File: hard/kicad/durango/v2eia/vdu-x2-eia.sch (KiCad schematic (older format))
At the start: 42 parts, among them Q4 BC548, Q5 BC548, U124 74HC574, U125 74HC157, U126 74HC86, U127 74HC245, U15 74HC4040, U16 74HC02, U17 74HC21, U18 74HC85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

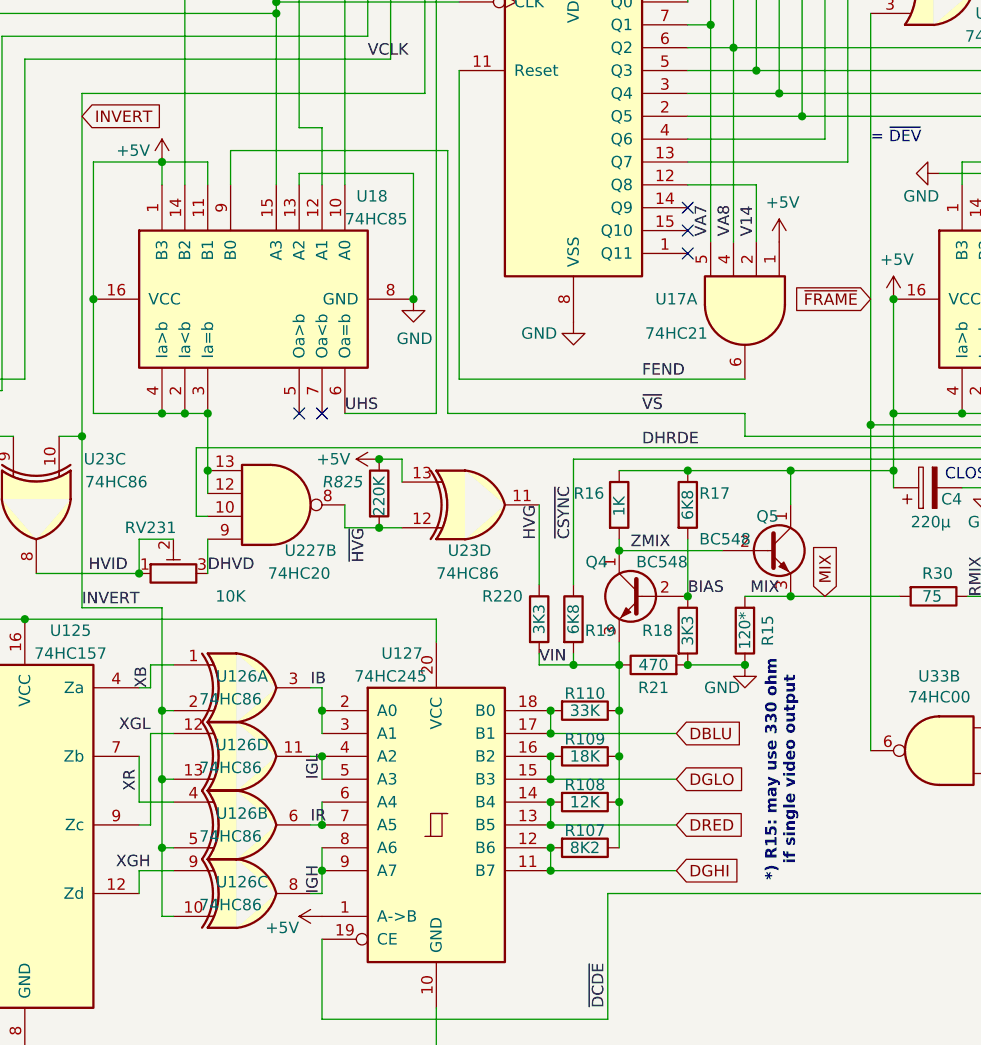
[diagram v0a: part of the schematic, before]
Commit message: fix EIA v2.2
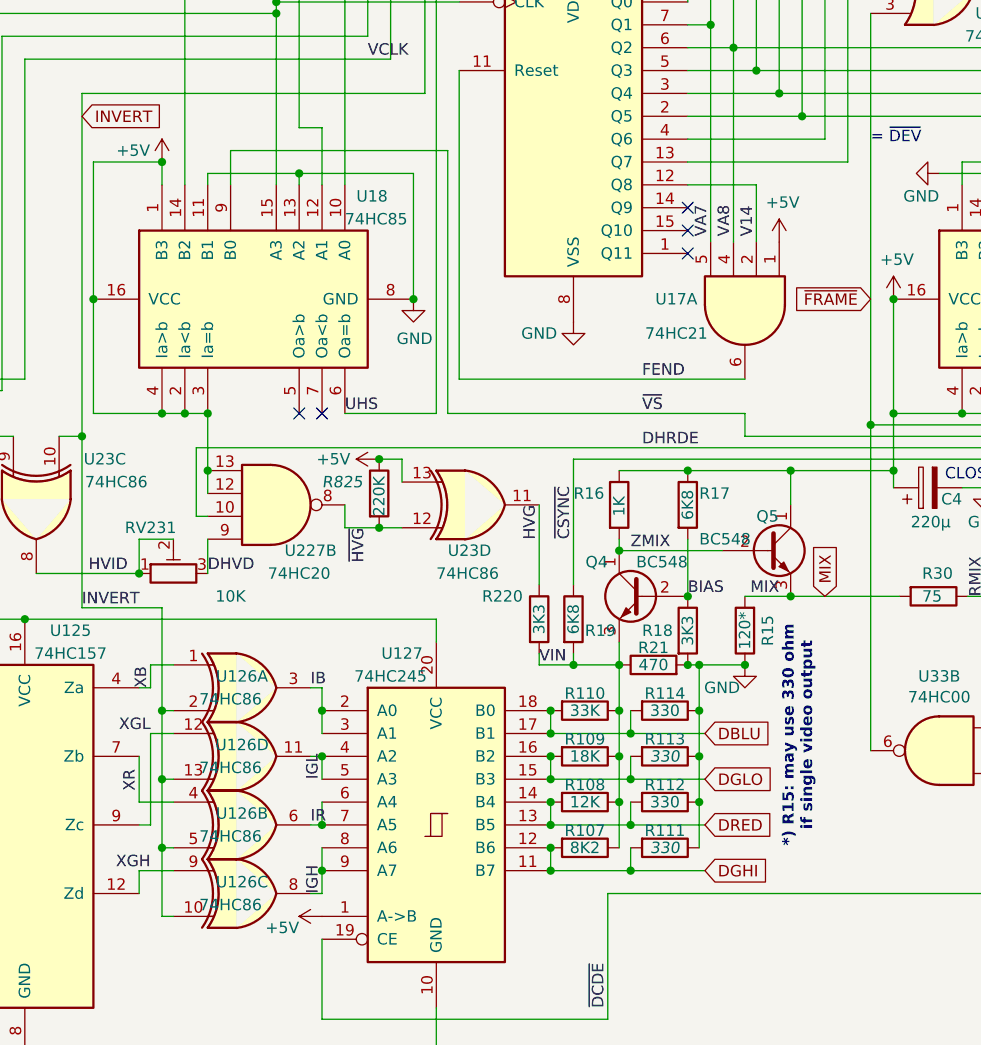
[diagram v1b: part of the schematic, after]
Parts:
- added R111, R112, R113, R114: 330, Resistor_THT:R_Axial_DIN0207_L6.3mm_D2.5mm_P2.54mm_Vertical, symbol Device:R
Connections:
- net +5V: no longer U18.11 (B1)
- net DBLU: now also R114.2
- net DGHI: now also R111.2
- net DGLO: now also R113.2
- net DRED: now also R112.2
- net GND: now also U18.11 (B1), R111.1, R112.1, R113.1, R114.1
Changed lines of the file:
@@
 $EndComp
 Wire Wire Line
-	6650 5800 7200 5800
-Wire Wire Line
-	6650 6000 7200 6000
-Wire Wire Line
-	6650 6200 7200 6200
-Wire Wire Line
-	7200 6400 6650 6400
+	6650 5800 7000 5800
+Wire Wire Line
+	6650 6000 7000 6000
+Wire Wire Line
+	6650 6200 7000 6200
+Wire Wire Line
+	7325 6400 7000 6400
 $Comp
 L Device:CP C5
@@
 U 1 1 60E10F90
 P 7100 5500
-F 0 "R21" V 7000 5500 50  0000 C CNN
+F 0 "R21" V 7175 5500 50  0000 C CNN
 F 1 "470" V 7100 5500 50  0000 C CNN
 F 2 "Resistor_THT:R_Axial_DIN0207_L6.3mm_D2.5mm_P2.54mm_Vertical" V 7030 5500 50  0001 C CNN
@@
 Text Label 7050 4250 0    50   ~ 0
 FEND
-Text Notes 7725 6450 1    50   ~ 10
+Text Notes 7800 6300 1    50   ~ 10
 *) R15: may use 330 ohm\n   if single video output
 $Comp
@@
 Connection ~ 3050 3450
 Wire Wire Line
-	7250 5500 7500 5500
+	7250 5500 7300 5500
 Wire Wire Line
 	6950 5000 7400 5000
@@
 	4950 3400 4950 3300
 Wire Wire Line
-	5150 3300 5150 3400
-Wire Wire Line
 	5550 3350 5550 3400
 Wire Wire Line
@@
 Text GLabel 2750 1300 2    50   Input ~ 0
 FCLK
-Text GLabel 7200 5800 2    50   Input ~ 0
+Text GLabel 7325 5800 2    50   Input ~ 0
 DBLU
-Text GLabel 7200 6000 2    50   Input ~ 0
+Text GLabel 7325 6000 2    50   Input ~ 0
 DGLO
-Text GLabel 7200 6200 2    50   Input ~ 0
+Text GLabel 7325 6200 2    50   Input ~ 0
 DRED
-Text GLabel 7200 6400 2    50   Input ~ 0
+Text GLabel 7325 6400 2    50   Input ~ 0
 DGHI
 Text Label 6600 5500 0    50   ~ 0
@@
 Text Label 9250 4700 0    50   ~ 0
 ~CSYNC
-Wire Wire Line
-	5150 3300 4950 3300
 Wire Wire Line
 	4850 5100 4850 4950
@@
 Wire Wire Line
 	1700 7550 1800 7550
-Wire Bus Line
-	8800 550  10750 550
-Wire Bus Line
-	4100 550  8050 550
-Wire Bus Line
-	800  4350 3700 4350
 $Comp
 L power:GND #PWR0178
@@
 Wire Wire Line
 	1800 7550 1900 7550
+$Comp
+L Device:R R114
+U 1 1 65BB1D73
+P 7150 5700
+F 0 "R114" V 7075 5700 50  0000 C CNN
+F 1 "330" V 7150 5700 50  0000 C CNN
+F 2 "Resistor_THT:R_Axial_DIN0207_L6.3mm_D2.5mm_P2.54mm_Vertical" V 7080 5700 50  0001 C CNN
+F 3 "~" H 7150 5700 50  0001 C CNN
+	1    7150 5700
+	0    1    1    0
+$EndComp
+$Comp
+L Device:R R113
+U 1 1 65BB4FC8
+P 7150 5900
+F 0 "R113" V 7075 5900 50  0000 C CNN
+F 1 "330" V 7150 5900 50  0000 C CIN
+F 2 "Resistor_THT:R_Axial_DIN0207_L6.3mm_D2.5mm_P2.54mm_Vertical" V 7080 5900 50  0001 C CNN
+F 3 "~" H 7150 5900 50  0001 C CNN
+	1    7150 5900
+	0    1    1    0
+$EndComp
+$Comp
+L Device:R R112
+U 1 1 65BB7467
+P 7150 6100
+F 0 "R112" V 7075 6100 50  0000 C CNN
+F 1 "330" V 7150 6100 50  0000 C CNN
+F 2 "Resistor_THT:R_Axial_DIN0207_L6.3mm_D2.5mm_P2.54mm_Vertical" V 7080 6100 50  0001 C CNN
+F 3 "~" H 7150 6100 50  0001 C CNN
+	1    7150 6100
+	0    1    1    0
+$EndComp
+$Comp
+L Device:R R111
+U 1 1 65BB86DA
+P 7150 6300
+F 0 "R111" V 7075 6300 50  0000 C CNN
+F 1 "330" V 7150 6300 50  0000 C CIN
+F 2 "Resistor_THT:R_Axial_DIN0207_L6.3mm_D2.5mm_P2.54mm_Vertical" V 7080 6300 50  0001 C CNN
+F 3 "~" H 7150 6300 50  0001 C CNN
+	1    7150 6300
+	0    1    1    0
+$EndComp
+Wire Wire Line
+	7000 6300 7000 6400
+Connection ~ 7000 6400
+Wire Wire Line
+	7000 6400 6650 6400
+Wire Wire Line
+	7000 6100 7000 6200
+Connection ~ 7000 6200
+Wire Wire Line
+	7000 6200 7325 6200
+Wire Wire Line
+	7000 5900 7000 6000
+Connection ~ 7000 6000
+Wire Wire Line
+	7000 6000 7325 6000
+Wire Wire Line
+	7000 5700 7000 5800
+Connection ~ 7000 5800
+Wire Wire Line
+	7000 5800 7325 5800
+Wire Wire Line
+	7300 6300 7300 6100
+Connection ~ 7300 5500
+Wire Wire Line
+	7300 5500 7500 5500
+Connection ~ 7300 5700
+Wire Wire Line
+	7300 5700 7300 5500
+Connection ~ 7300 5900
+Wire Wire Line
+	7300 5900 7300 5700
+Connection ~ 7300 6100
+Wire Wire Line
+	7300 6100 7300 5900
+Wire Wire Line
+	5550 3350 5150 3350
+Wire Wire Line
+	5150 3350 5150 3400
+Connection ~ 5550 3350
+Wire Bus Line
+	8800 550  10750 550
+Wire Bus Line
+	4100 550  8050 550
+Wire Bus Line
+	800  4350 3700 4350
 $EndSCHEMATC
